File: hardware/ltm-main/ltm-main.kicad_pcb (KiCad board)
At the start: 2 copper layers, 94 x 84 mm, 34 parts, among them J1 BATERAI (dari BMS), J2 MOTOR KIRI, J3 MOTOR KANAN, J4 OLED 1.3in I2C, J5 KE PCB SENSOR, Q1 S8050, SW1 ON/OFF, SW2 A (MENU), SW3 B (OK), U1 ESP32 DevKit 30P CH340, U2 TB6612FNG, U3 MP1584 (5,0 V)

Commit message: Model 3D v11 disamakan dengan layout PCB v1; area ball caster bebas kaki solder
- Model: lubang H3/H4 dan spacer antar papan, pangkal leher sensor ±14, saklar + JST XH baterai di tepi
  kiri, JST motor, buzzer, elko, resistor/kapasitor, socket OLED 8,5 mm, pin J5, komponen bawah PCB sensor
- Dinding motor berhenti sebelum tepi belakang PCB utama (sebelumnya beririsan 1 mm)
- PCB: R3/R4 dan R5-R8 digeser keluar area ball caster, tanda caster & BMS di silkscreen bawah, routing ulang
- STEP, render mekanik, dan render PCB diperbarui

Co-Authored-By: Claude Opus 5.5 <noreply@anthropic.com>
Claude-Session: https://claude.ai/code/session_016j7fGnGXJh3ke3RU3C9DKW
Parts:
- moved R3 3.00 mm to (107.0, 89.0)
- moved R4 3.00 mm to (107.0, 93.0)
- moved R5 2.50 mm to (83.5, 88.0)
- moved R6 2.50 mm to (86.5, 88.0)
- moved R7 2.50 mm to (89.5, 88.0)
- moved R8 2.50 mm to (92.5, 88.0)
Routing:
- net /VBAT: track 172.8 -> 144.5 mm, vias 2 -> 1
- net /PWMB: track 94.2 -> 75.2 mm, vias 2 -> 0
- net /MR_N: track 97.7 -> 80.2 mm
- net /VBAT_SENSE: track 42.2 -> 58.9 mm
- net /S2: track 93.8 -> 77.9 mm, vias 1 -> 3
- net /PWMA: track 70.7 -> 58.8 mm, vias 0 -> 1
- net /AIN2: track 73.7 -> 61.9 mm, vias 2 -> 0
- net /ENC_L_A: track 77.5 -> 85.5 mm, vias 3 -> 2
- net GND: track 358.4 -> 350.3 mm, vias 0 -> 1
- net +3V3: track 180.1 -> 173.5 mm
- net /SDA: track 11.4 -> 4.88 mm
- net /IR_EN: track 79.2 -> 85.7 mm
- net /BTN_A: track 78.6 -> 81.7 mm, vias 1 -> 0
- net /S4: track 75.5 -> 72.8 mm
- net /AIN1: track 63.9 -> 61.4 mm
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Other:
- board text added: "BMS 2S (ditempel di sini)"
- board text added: "CASTER"

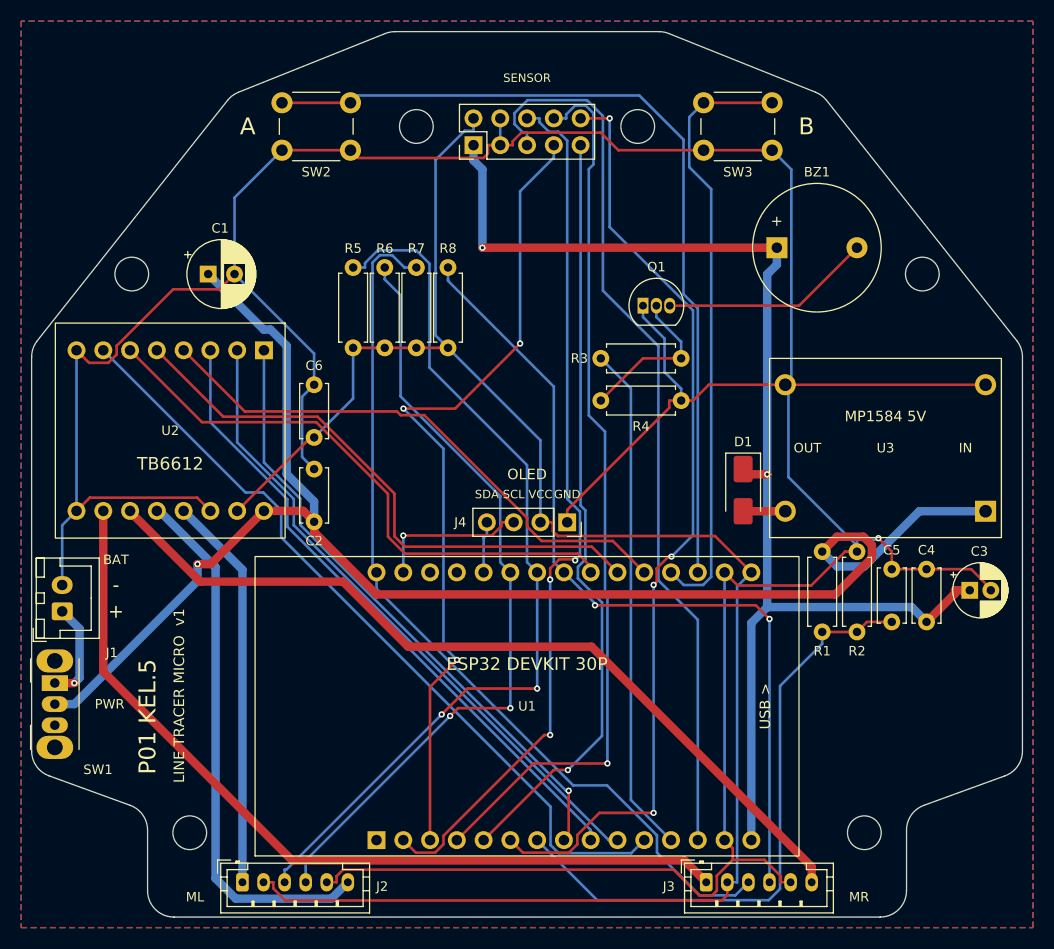
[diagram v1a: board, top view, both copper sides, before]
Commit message: PCB utama v2: lebih sederhana dan gampang diakses untuk edukasi
- Skematik 34 -> 25 komponen: C2-C6 dan R5-R8 dibuang (modul sudah punya
  kapasitor, encoder pakai INPUT_PULLUP), D1 SS14 -> 1N5819 (semua THT).
- ESP32 keluar dari bawah dudukan baterai, ESP32/TB6612/OLED di socket,
  MP1584 + D1 + R1/R2 di bawah dudukan baterai, J1/SW1 di tepi kanan.
- OLED header di depan: layar tidak perlu diputar (U8G2_R0).
- Silkscreen kotak blok (DAYA, OTAK, DRIVER MOTOR, LAYAR, SUARA) + peta
  ALUR DAYA. DRC 0/0, 294 segmen, 9 via.
- Model 3D v12 ikut PCB utama v2; tepi dudukan baterai ke Y 29,5.

Co-Authored-By: Claude Opus 5.5 <noreply@anthropic.com>
Claude-Session: https://claude.ai/code/session_016j7fGnGXJh3ke3RU3C9DKW
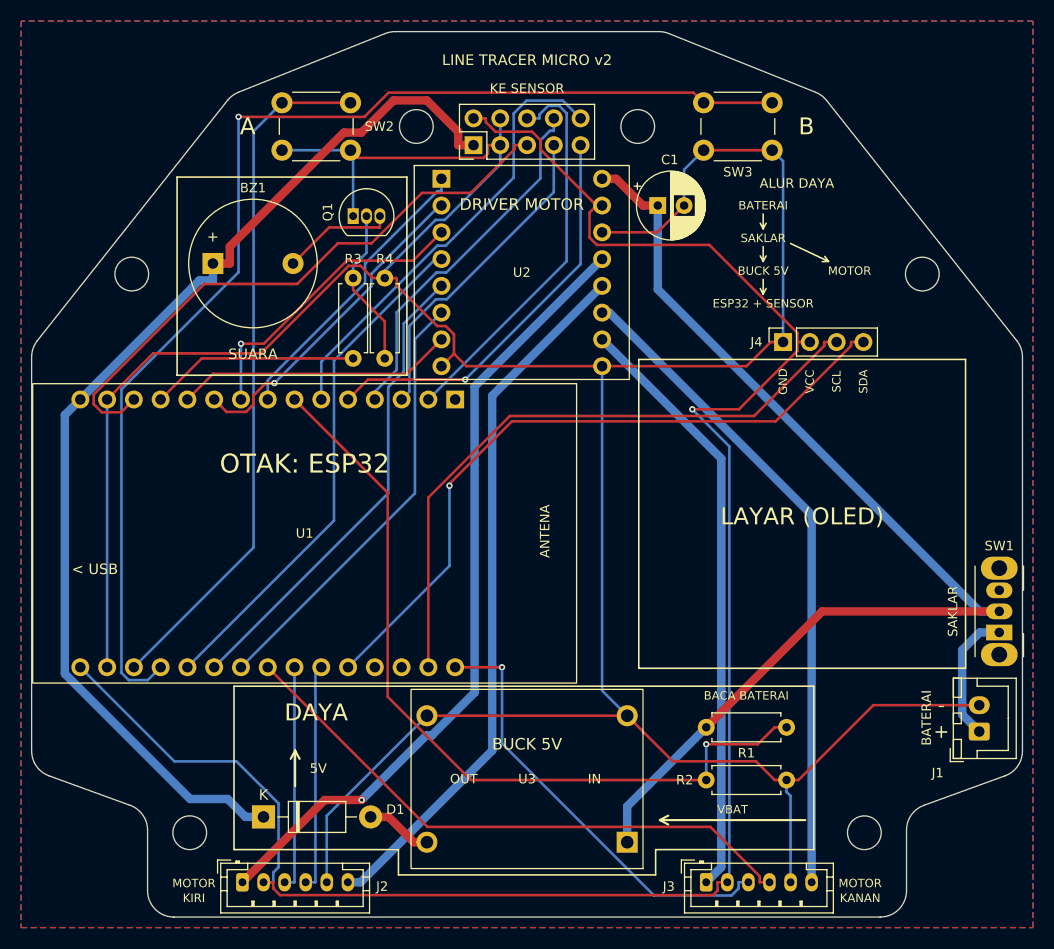
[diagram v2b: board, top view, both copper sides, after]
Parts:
- removed C2, C4, C5, C6: 100nF, Capacitor_THT:C_Disc_D5.0mm_W2.5mm_P5.00mm
- removed C3: 10uF/16V, Capacitor_THT:CP_Radial_D5.0mm_P2.00mm
- removed R5, R6, R7, R8: 10k, Resistor_THT:R_Axial_DIN0207_L6.3mm_D2.5mm_P7.62mm_Horizontal
- D1: value SS14 -> 1N5819; footprint Diode_SMD:D_SMA -> Diode_THT:D_DO-41_SOD81_P10.16mm_Horizontal
- moved SW1 89.7 mm to (144.8, 115.0), turned to 90 degrees
- moved J1 87.7 mm to (142.9, 124.4)
- moved D1 55.1 mm to (75.0, 132.5), turned to 0 degrees
- moved BZ1 53.5 mm to (70.2, 80.0)
- moved U3 46.3 mm to (100.0, 128.9)
- moved C1 43.1 mm to (112.4, 74.5)
- moved U2 36.6 mm to (99.5, 80.8), turned to 0 degrees
- moved U1 32.5 mm to (75.4, 105.6), turned to -90 degrees
- moved Q1 28.8 mm to (83.5, 75.5)
- moved J4 26.7 mm to (124.3, 87.5), turned to 90 degrees
- moved R3 23.5 mm to (83.5, 89.0), turned to 90 degrees
- moved R4 20.9 mm to (86.5, 89.0), turned to 90 degrees
- moved R2 20.0 mm to (117.0, 129.0), turned to 0 degrees
- moved R1 20.0 mm to (117.0, 124.0), turned to 0 degrees
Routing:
- net /ENC_L_A: track 85.5 -> 21.3 mm, vias 2 -> 0
- net /SDA: track 4.88 -> 66.4 mm, vias 0 -> 1
- net /BTN_B: track 57.5 -> 113.8 mm, vias 0 -> 1
- net /ENC_L_B: track 74.2 -> 21.6 mm, vias 2 -> 0
- net /S3: track 84.7 -> 34.5 mm, vias 1 -> 0
- net /PWMB: track 75.2 -> 26.5 mm
- net /S2: track 77.9 -> 30.7 mm, vias 3 -> 0
- net /S5: track 89.8 -> 42.7 mm, vias 4 -> 0
- net /SCL: track 14.7 -> 61.2 mm, vias 1 -> 0
- net /S1: track 83.5 -> 37.3 mm, vias 3 -> 0
- net /ENC_R_A: track 84.8 -> 41.9 mm, vias 0 -> 1
- net /VBAT: track 144.5 -> 105.7 mm, vias 1 -> 0
- net /ML_P: track 37.5 -> 75.6 mm, vias 0 -> 1
- net GND: track 350.3 -> 313.0 mm, vias 1 -> 0
- net /S4: track 72.8 -> 38.7 mm
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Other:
- board text added: "5V"
- board text added: "< USB"
- board text added: "ALUR DAYA"
- board text added: "ANTENA"
- board text added: "BACA BATERAI"
- board text added: "BATERAI"
- board text added: "BUCK 5V"
- board text added: "DAYA"
- board text added: "DRIVER MOTOR"
- board text added: "ESP32 + SENSOR"
- board text added: "KANAN"
- board text added: "KE SENSOR"
- board text added: "KIRI"
- board text added: "LAYAR (OLED)"
- board text added: "LINE TRACER MICRO v2"
- board text added: "MOTOR"
- board text added: "OTAK: ESP32"
- board text added: "PjBL DTEO FV ITS 2026"
- board text added: "SAKLAR"
- board text added: "SUARA"
- board text added: "VBAT"
- board text removed: "BAT"
- board text removed: "ESP32 DEVKIT 30P"
- board text removed: "LINE TRACER MICRO v1"
- board text removed: "ML"
- board text removed: "MP1584 5V"
- board text removed: "MR"
- board text removed: "OLED"
- board text removed: "PWR"
- board text removed: "SENSOR"
- board text removed: "TB6612"
- board text removed: "USB >"

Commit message: Sensor 16 titik + mux + LED, kabel pita, aturan cetak 0,8 mm
- PCB sensor v2: batang lurus 110 x 51 mm, 16x ITR20001 (jarak 6,5 mm),
  modul mux CD74HC4067, MCP23017 + 16 LED indikator, box header IDC J1
- PCB utama: J5 jadi box header IDC 2x6 (kabel pita ke PCB sensor),
  pin ESP32 disusun ulang supaya jalur tidak saling silang
- Aturan tempat cetak: jalur >= 0,8 mm (daya 1,2), clearance 0,5,
  via 1,6/0,8; kedua PCB 0 jalur putus, DRC bersih
- Charter/RAB: 16 sensor, total Rp896.000
- Model 3D v12: PCB sensor batang di dudukan 3D print + kabel pita,
  STEP dan render diperbarui

Co-Authored-By: Claude Opus 5.5 <noreply@anthropic.com>
Claude-Session: https://claude.ai/code/session_016j7fGnGXJh3ke3RU3C9DKW
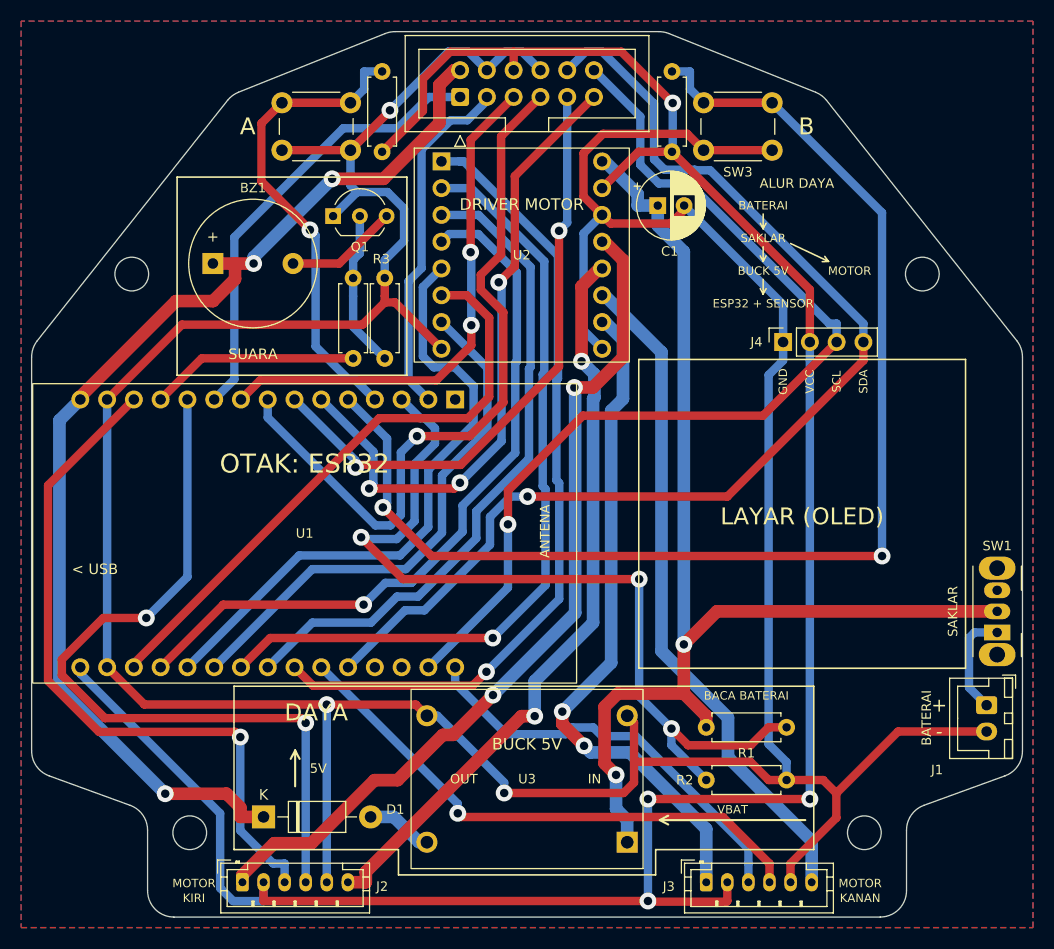
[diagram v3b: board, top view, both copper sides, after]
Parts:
- removed H5, H6: M3, MountingHole:MountingHole_3.2mm_M3
- added R5: 10k, Resistor_THT:R_Axial_DIN0207_L6.3mm_D2.5mm_P7.62mm_Horizontal, F.Cu at (86.2, 69.4)
- added R6: 10k, Resistor_THT:R_Axial_DIN0207_L6.3mm_D2.5mm_P7.62mm_Horizontal, F.Cu at (113.8, 69.4)
- J5: footprint Connector_PinHeader_2.54mm:PinHeader_2x05_P2.54mm_Vertical -> Connector_IDC:IDC-Header_2x06_P2.54mm_Vertical
- Q1: footprint Package_TO_SOT_THT:TO-92_Inline -> Package_TO_SOT_THT:TO-92_Inline_Wide
- moved J5 4.74 mm to (93.7, 64.2)
- moved J1 2.60 mm to (143.6, 121.9), turned to -90 degrees
- moved Q1 1.90 mm to (81.6, 75.5)
- moved U2 1.65 mm to (99.5, 79.2)
- moved SW1 0.20 mm to (144.6, 115.0)
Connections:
- J5 pad 1: +5V -> /IR_EN
- J5 pad 10: /S5 -> /SDA
- J5 pad 2: +3V3 -> +5V
- J5 pad 3: GND -> /SIG
- J5 pad 5: /IR_EN -> /MUX_S0
- J5 pad 6: /S1 -> +3V3
- J5 pad 7: /S2 -> /MUX_S1
- J5 pad 8: /S3 -> GND
- J5 pad 9: /S4 -> /MUX_S2
- U1 pad 10: /AIN2 -> /IR_EN
- U1 pad 11: /PWMB -> /ENC_L_B
- U1 pad 13: /IR_EN -> /ENC_L_A
- U1 pad 2: /S1 -> /SIG
- U1 pad 21: /ENC_L_B -> /ENC_R_B
- U1 pad 22: /ENC_L_A -> /PWMA
- U1 pad 23: /ENC_R_B -> /AIN1
- U1 pad 24: /BIN2 -> /AIN2
- U1 pad 25: /BIN1 -> /PWMB
- U1 pad 26: /STBY -> /BIN1
- U1 pad 27: /BTN_B -> /STBY
- U1 pad 28: /BTN_A -> /BIN2
- U1 pad 3: /S2 -> /VBAT_SENSE
- U1 pad 4: /S3 -> /BTN_A
- U1 pad 5: /S4 -> /BTN_B
- U1 pad 6: /S5 -> /MUX_S3
- U1 pad 7: /VBAT_SENSE -> /MUX_S2
- U1 pad 8: /PWMA -> /MUX_S1
- U1 pad 9: /AIN1 -> /MUX_S0
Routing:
- net /MUX_S1: track 0.00 -> 68.8 mm, vias 0 -> 1
- net /MUX_S3: track 0.00 -> 61.6 mm, vias 0 -> 3
- net /MUX_S2: track 0.00 -> 58.0 mm, vias 0 -> 2
- net /ENC_L_B: track 21.6 -> 73.6 mm, vias 0 -> 2
- net /MUX_S0: track 0.00 -> 49.3 mm, vias 0 -> 2
- net /PWMA: track 28.0 -> 76.8 mm, vias 0 -> 1
- net /ENC_L_A: track 21.3 -> 66.7 mm, vias 0 -> 1
- net /AIN2: track 31.3 -> 75.6 mm
- net /S5: track 42.7 -> 0.00 mm
- net /SDA: track 66.4 -> 108.6 mm
- net +3V3: track 183.3 -> 222.1 mm, vias 1 -> 4
- net /S4: track 38.7 -> 0.00 mm, vias 1 -> 0
- net GND: track 313.0 -> 351.2 mm, vias 0 -> 3
- net /S1: track 37.3 -> 0.00 mm
- net /AIN1: track 28.7 -> 63.2 mm, vias 1 -> 0
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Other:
- board text removed: "KE SENSOR"
